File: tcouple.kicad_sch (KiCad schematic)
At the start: 3 parts, among them U7 MAX31855KASA

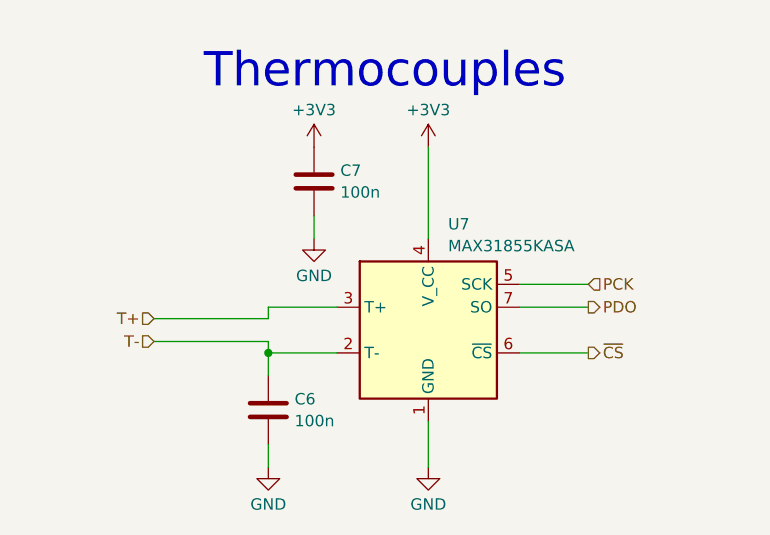
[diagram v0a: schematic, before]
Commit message: Further work, most components now present
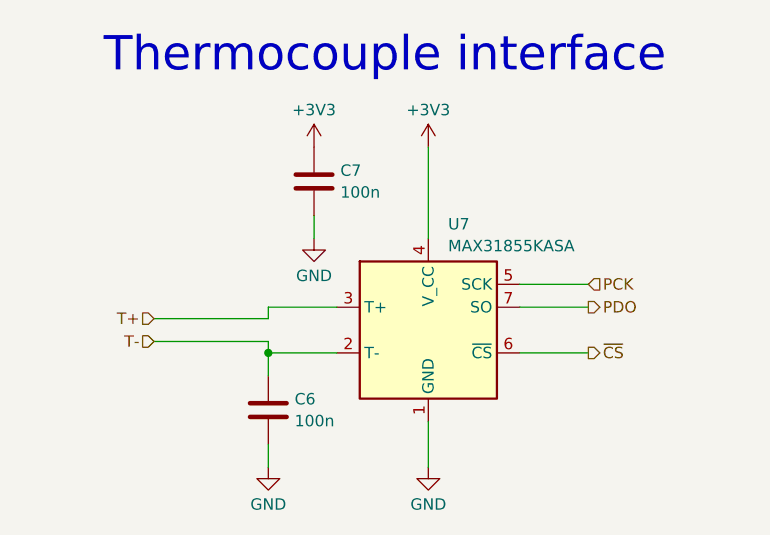
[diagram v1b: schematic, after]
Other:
- note added: "Thermocouple interface"
- note removed: "Thermocouples"
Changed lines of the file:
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@@
 		)
 	)
-	(text "Thermocouples"
+	(text "Thermocouple interface"
 		(exclude_from_sim no)
-		(at 128.524 65.278 0)
+		(at 128.524 63.5 0)
 		(effects
 			(font
